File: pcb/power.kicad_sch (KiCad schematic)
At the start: 17 parts, among them J10 Screw_Terminal_01x02, J11 Screw_Terminal_01x02, J12 Conn_01x02, J13 Conn_01x02, J14 Conn_01x02, J34 Screw_Terminal_01x02, J35 Conn_01x02, J36 Conn_01x02, J4 Screw_Terminal_01x02, J7 Screw_Terminal_01x02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

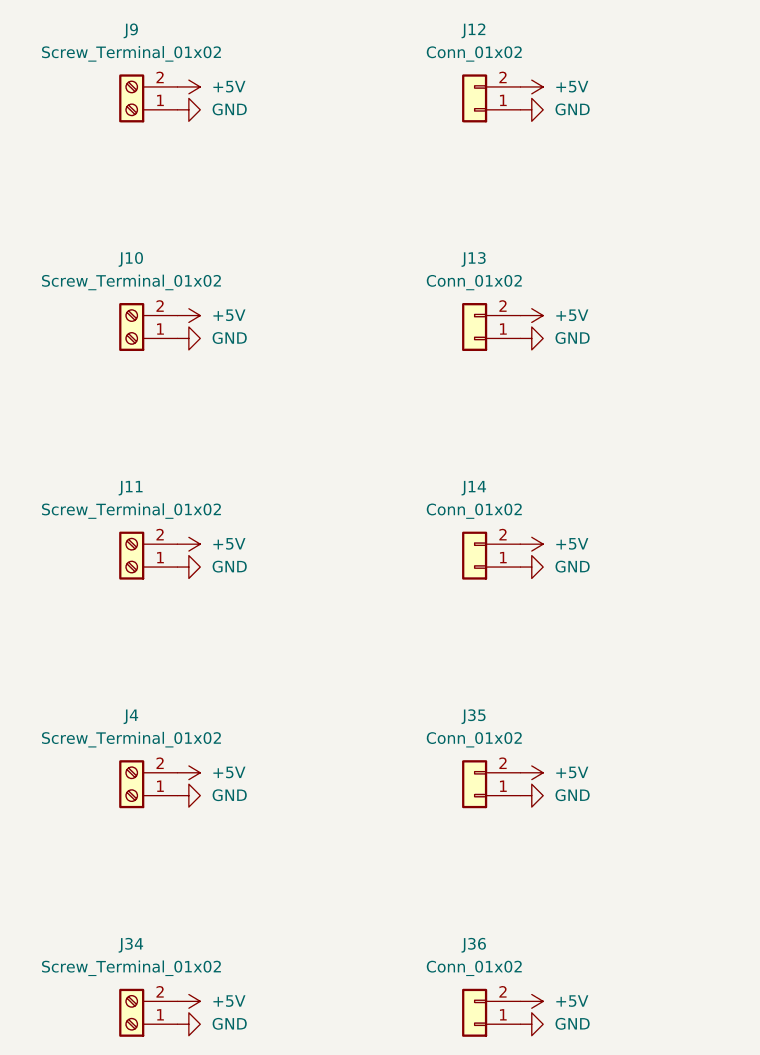
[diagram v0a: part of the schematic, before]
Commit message: Use larger screw terminals, adjust layout to suit
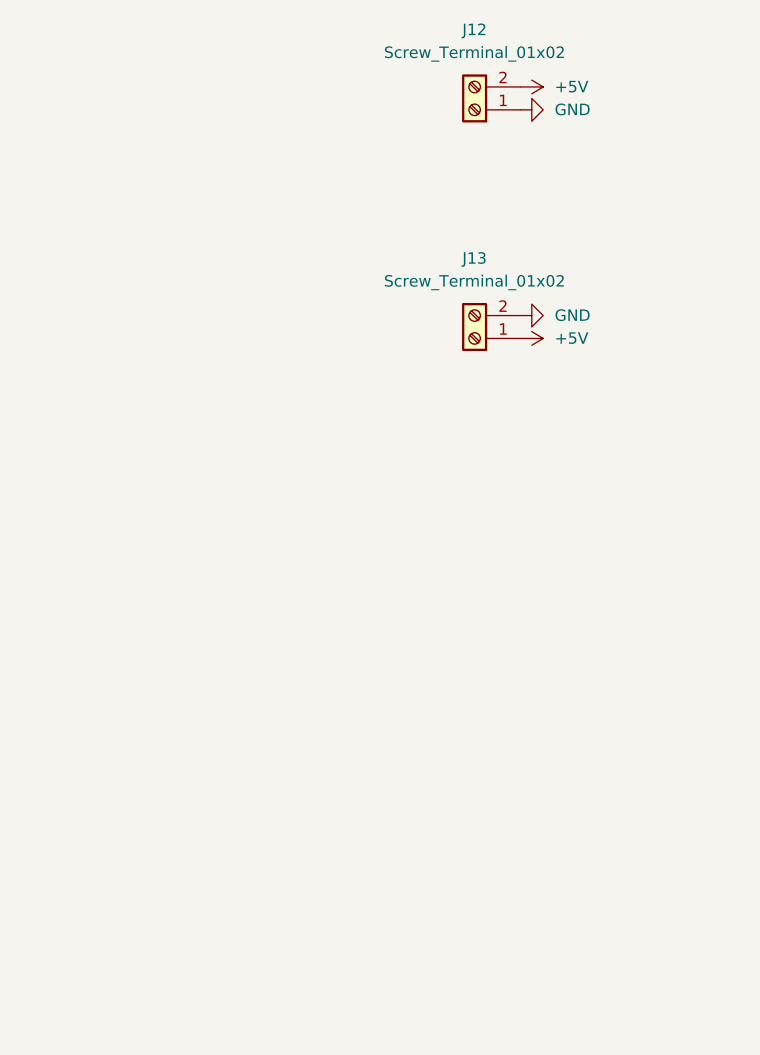
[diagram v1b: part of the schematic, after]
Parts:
- removed J10, J11, J34, J4, J9: Screw_Terminal_01x02, Conn_ScrewTerminals:ED5552DS, symbol Connector:Screw_Terminal_01x02
- removed J14, J35, J36: Conn_01x02, Connector_PinHeader_2.54mm:PinHeader_1x02_P2.54mm_Vertical, symbol Connector_Generic:Conn_01x02
- J12, J13: value Conn_01x02 -> Screw_Terminal_01x02; footprint Connector_PinHeader_2.54mm:PinHeader_1x02_P2.54mm_Vertical -> Conn_ScrewTerminals:CTB7000-2; symbol Connector_Generic:Conn_01x02 -> Connector:Screw_Terminal_01x02
- J7: footprint Conn_ScrewTerminals:ED5552DS -> Conn_ScrewTerminals:CTB7000-2
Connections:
- net +5V: now also J13.1 (Pin_1); no longer J13.2 (Pin_2)
- net GND: now also J13.2 (Pin_2); no longer J13.1 (Pin_1)
